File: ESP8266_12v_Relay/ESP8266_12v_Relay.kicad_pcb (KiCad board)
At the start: 2 copper layers, 71.9 x 40.9 mm, 41 parts, among them J1 691137710002, J2 691137710002, J3 691137710002, J4 691137710002, J5 Conn_01x06_Female, J6 691137710002, U1 ESP-WROOM-02D_M1102H3200PH3Q0_, U2 AP6502SP-13, U3 DMN2029USD-13, U4 DMN2029USD-13

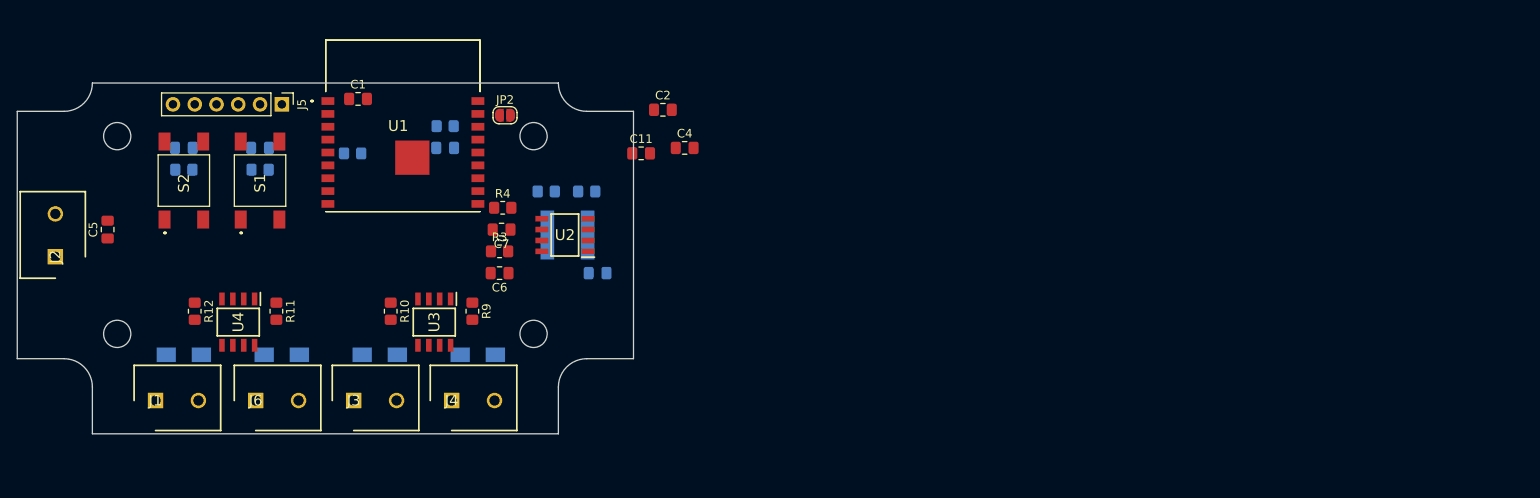
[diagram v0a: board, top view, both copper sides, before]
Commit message: Started 12v relay design
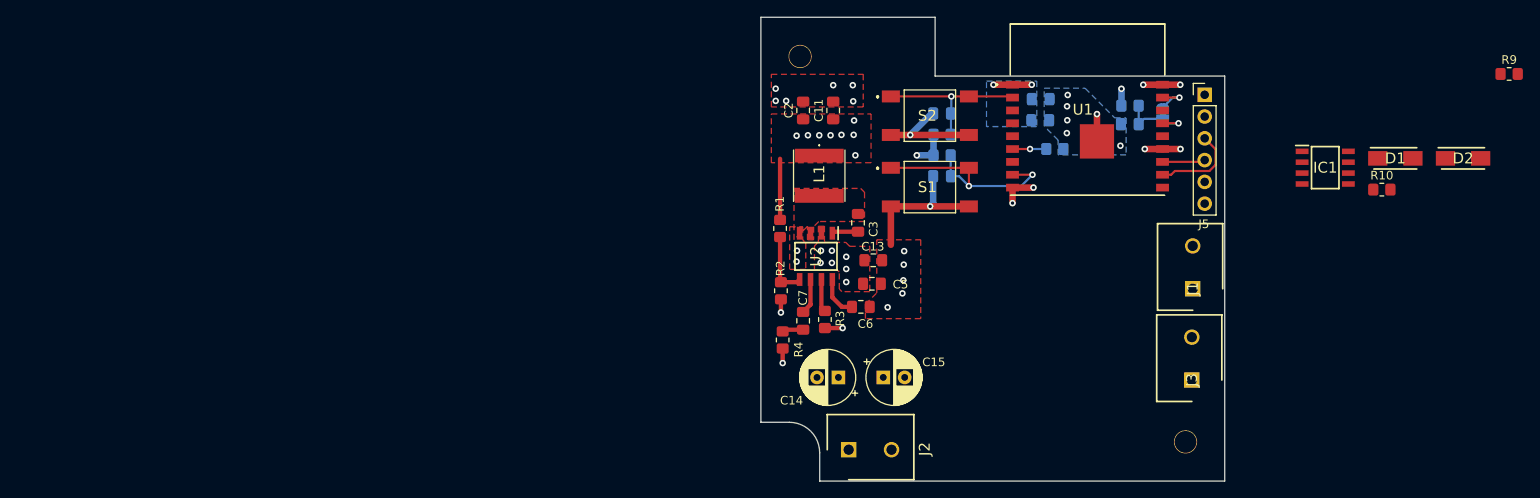
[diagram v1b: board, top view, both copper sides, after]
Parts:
- removed D3, D4: FM4004W-W, SamacSys_Parts:DIOM5025X231N
- removed J4, J6: 691137710002, SamacSys_Parts:SHDR2W70P0X500_1X2_1000X750X1160P
- removed R11, R12: 10k, Resistor_SMD:R_0805_2012Metric_Pad1.20x1.40mm_HandSolder
- removed U3, U4: DMN2029USD-13, SamacSys_Parts:SOIC127P600X175-8N
- added C13: 10uF, Capacitor_SMD:C_0805_2012Metric_Pad1.18x1.45mm_HandSolder, F.Cu at (216.3, 104.5)
- added C14: 100uF, Capacitor_THT:CP_Radial_D6.3mm_P2.50mm, F.Cu at (212.2, 118.2)
- added C15: 100uF, Capacitor_THT:CP_Radial_D6.3mm_P2.50mm, F.Cu at (217.5, 118.2)
- added H1: MountingHole, MountingHole:MountingHole_2.7mm_M2.5, F.Cu at (207.8, 80.8)
- added H2: MountingHole, MountingHole:MountingHole_2.7mm_M2.5, F.Cu at (252.7, 125.7)
- added IC1: DMN2029USD-13, SamacSys_Parts:SOIC127P600X175-8N, F.Cu at (269.0, 93.7)
- C1, C4, JP2: moved to B.Cu
- C11: value 10uF -> 22uF
- C3, D1, D2, L1, R1, R2: moved to F.Cu
- moved D1 143.2 mm to (277.2, 92.7)
- moved D2 139.7 mm to (285.1, 92.7)
- moved R9 124.1 mm to (290.5, 82.8), turned to 0 degrees
- moved J1 121.7 mm to (253.6, 107.9), turned to 90 degrees
- moved R10 116.5 mm to (275.6, 96.3), turned to 0 degrees
- moved J5 107.7 mm to (255.0, 85.2), turned to 0 degrees
- moved J3 97.8 mm to (253.5, 118.5), turned to 90 degrees
- moved J2 95.2 mm to (213.4, 126.6), turned to 0 degrees
- moved C5 89.4 mm to (216.2, 107.3), turned to 0 degrees
- moved R5 88.5 mm to (224.3, 89.9)
- moved C8 88.5 mm to (224.3, 87.4), turned to 180 degrees
- moved S2 87.3 mm to (222.9, 87.7), turned to 0 degrees
- moved R8 81.9 mm to (237.5, 91.6)
- moved R6 79.9 mm to (246.3, 86.5)
- moved C9 79.9 mm to (246.2, 88.7)
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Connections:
- net /ESP_TOUT renamed /TOUT
- C11 pad 1: +12V -> +3V3
- J1 pad 2: /PWM3_D -> /PWM0_D
- U1 pad 6: /PWM2 -> /GPIO15
- U1 pad 7: /PWM3 -> /GPIO2
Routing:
- net GND: track 0.00 -> 49.2 mm, vias 0 -> 29
- net /GPIO0: track 0.00 -> 26.5 mm, vias 0 -> 2
- net /ESP_EN: track 0.00 -> 18.7 mm, vias 0 -> 1
- net +3V3: track 0.00 -> 17.9 mm, vias 0 -> 12
- net /ESP_RXD: track 0.00 -> 10.3 mm
- net /ESP_RST_L: track 0.00 -> 9.15 mm, vias 0 -> 1
- net /U2_FB: track 0.00 -> 7.62 mm
- net /ESP_TXD: track 0.00 -> 5.00 mm
- net /U2_SS: track 0.00 -> 4.83 mm
- net /GPIO16: track 0.00 -> 4.41 mm, vias 0 -> 1
- net /U2_COMP: track 0.00 -> 4.14 mm
- net /GPIO15: track 0.00 -> 3.94 mm, vias 0 -> 1
- net /U2_EN: track 0.00 -> 3.83 mm
- net /U2_BST: track 0.00 -> 3.07 mm
- net Net-(C7-Pad2): track 0.00 -> 2.47 mm
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- added copper zone on F.Cu, net +12V
- added copper zone on In2.Cu, net +12V
- added copper zone on B.Cu, net +3V3
- added copper zone on F.Cu, net +3V3
- added copper zone on In2.Cu, net +3V3
- added copper zone on F.Cu, net /U2_SW
- added copper zone on B.Cu, net GND
- added copper zone on F.Cu, net GND
- added copper zone on In1.Cu, net GND
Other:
- board size 71.9 x 40.9 mm -> 54.1 x 54.1 mm
- copper layers 2 -> 4
- net class Default: clearance 0.1524 -> 0.254; trace_width 0.1524 -> 0.254; via_dia 0.508 -> 0.5588
- net class Power added: clearance 0.508, trace_width 0.508, via_dia 0.762, via_drill 0.508
- rule trace_clearance: 0.1524 -> 0.254
- rule trace_min: 0.1524 -> 0.254
- rule via_min_size: 0.508 -> 0.5588
- board text removed: "Adafruit MPU6050"

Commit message: Finished 12v relay layout
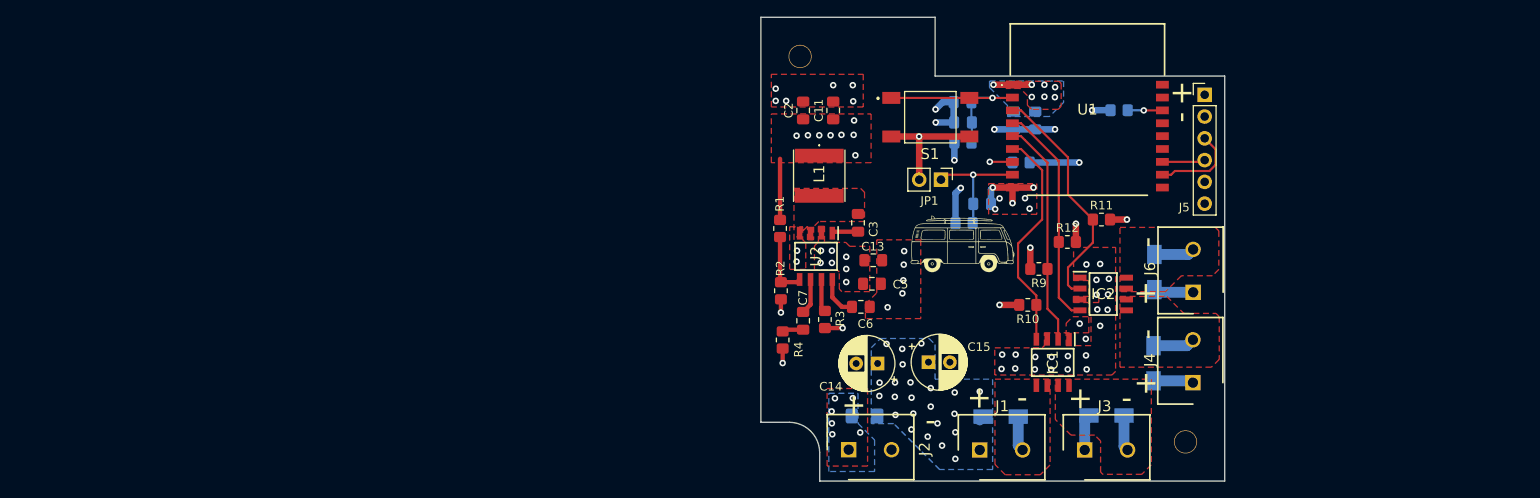
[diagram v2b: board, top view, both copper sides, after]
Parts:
- removed JP2: SolderJumper_2_Open, Jumper:SolderJumper-2_P1.3mm_Open_RoundedPad1.0x1.5mm
- removed S2: LL3301NF065QG, SamacSys_Parts:LL3301NF065QG
- added D3: FM4004W-W, SamacSys_Parts:DIOM5025X231N, B.Cu at (249.1, 105.9)
- added D4: FM4004W-W, SamacSys_Parts:DIOM5025X231N, B.Cu at (249.0, 116.6)
- added F1: 5A, Fuse:Fuse_1206_3216Metric_Pad1.42x1.75mm_HandSolder, B.Cu at (215.3, 122.7)
- added G1: Van_Graphic, SamacSys_Parts:van_pic, F.Cu at (226.7, 102.6)
- added IC2: DMN2029USD-13, SamacSys_Parts:SOIC127P600X175-8N, F.Cu at (243.1, 108.5)
- added J4: 691137710002, SamacSys_Parts:SHDR2W70P0X500_1X2_1000X750X1160P, F.Cu at (253.6, 118.8)
- added J6: 691137710002, SamacSys_Parts:SHDR2W70P0X500_1X2_1000X750X1160P, F.Cu at (253.6, 108.3)
- added JP1: Jumper_2_Open, Connector_PinHeader_2.54mm:PinHeader_1x02_P2.54mm_Vertical, F.Cu at (224.2, 95.1)
- added R11: 10k, Resistor_SMD:R_0805_2012Metric_Pad1.20x1.40mm_HandSolder, F.Cu at (242.9, 99.8)
- added R12: 10k, Resistor_SMD:R_0805_2012Metric_Pad1.20x1.40mm_HandSolder, F.Cu at (238.9, 102.4)
- C8: value 0.1uF -> 1uF
- D1, D2: moved to B.Cu
- U1: value ESP-WROOM-02D_M1102H3200PH3Q0_ -> ESP32-C3-WROOM-02-H4; footprint SamacSys_Parts:ESPWROOM02DM1102H3200PH3Q0 -> SamacSys_Parts:ESP32C3WROOM02H4
- moved D2 61.8 mm to (231.2, 122.8)
- moved R9 59.4 mm to (235.6, 105.6), turned to 180 degrees
- moved D1 45.1 mm to (243.5, 122.7)
- moved R10 43.4 mm to (234.3, 109.8), turned to 180 degrees
- moved IC1 39.1 mm to (237.2, 116.5), turned to 270 degrees
- moved J1 26.0 mm to (228.7, 126.7), turned to 0 degrees
- moved J3 22.6 mm to (241.0, 126.7), turned to 0 degrees
- moved R5 20.8 mm to (245.0, 87.0)
- moved C9 19.7 mm to (226.7, 86.1)
- moved R6 14.3 mm to (233.6, 93.1), turned to 180 degrees
- moved U1 13.8 mm to (231.8, 97.0)
- moved R8 10.7 mm to (226.8, 90.8)
- moved R7 8.31 mm to (226.9, 100.2)
- moved S1 8.15 mm to (223.0, 87.9)
- moved C10 5.68 mm to (229.0, 98.0), turned to 0 degrees
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- renumbered J3 to J1, J1 to J3
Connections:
- net /GPIO4 renamed /GPIO10_NC
- net /GPIO5 renamed /GPIO19_NC
- C10 pad 1: /GPIO0 -> /GPIO9
- C9 pad 1: /ESP_RST_L -> /ESP_EN
- D1 pad 2: /PWM0_D -> /PWM1_D
- D2 pad 2: /PWM1_D -> /PWM0_D
- IC1 pad 2: /PWM0 -> /PWM1
- IC1 pad 4: /PWM1 -> /PWM0
- IC1 pad 5: /PWM1_D -> /PWM0_D
- IC1 pad 6: /PWM1_D -> /PWM0_D
- IC1 pad 7: /PWM0_D -> /PWM1_D
- IC1 pad 8: /PWM0_D -> /PWM1_D
- J1 pad 2: /PWM1_D -> /PWM0_D
- J2 pad 1: +12V -> Net-(F1-Pad1)
- J3 pad 2: /PWM0_D -> /PWM1_D
- R10 pad 1: /PWM1 -> /PWM0
- R5 pad 2: /ESP_EN -> /GPIO2
- R6 pad 2: /ESP_RST_L -> /GPIO8
- R7 pad 2: /GPIO0 -> /GPIO9
- R8 pad 1: /GPIO15 -> +3V3
- R8 pad 2: GND -> /ESP_EN
- R9 pad 1: /PWM0 -> /PWM1
- S1 pad 1: /GPIO0 -> /ESP_EN
- S1 pad 2: /GPIO0 -> /ESP_EN
- U1 pad 13: GND -> /GPIO18_NC
- U1 pad 15: /ESP_RST_L -> /GPIO3_NC
- U1 pad 16: /TOUT -> /GPIO2
- U1 pad 17: /GPIO16 -> /GPIO1_NC
- U1 pad 18: GND -> /GPIO0_NC
- U1 pad 3: /GPIO14 -> /PWM3
- U1 pad 4: /PWM0 -> /PWM2
- U1 pad 6: /GPIO15 -> /PWM0
- U1 pad 7: /GPIO2 -> /GPIO8
- U1 pad 8: /GPIO0 -> /GPIO9
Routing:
- net /PWM3: track 0.00 -> 27.6 mm
- net /GPIO0: track 26.5 -> 0.00 mm, vias 2 -> 0
- net /PWM1: track 0.00 -> 26.5 mm
- net /PWM0: track 0.00 -> 26.3 mm
- net /PWM2: track 0.00 -> 26.3 mm
- net /GPIO9: track 0.00 -> 14.4 mm, vias 0 -> 1
- net +12V: track 2.07 -> 16.2 mm, vias 8 -> 31
- net /ESP_RST_L: track 9.15 -> 0.00 mm, vias 1 -> 0
- net +3V3: track 17.9 -> 25.9 mm, vias 12 -> 19
- net /PWM2_D: track 0.00 -> 4.88 mm
- net /PWM3_D: track 0.00 -> 4.76 mm
- net /GPIO16: track 4.41 -> 0.00 mm, vias 1 -> 0
- net /PWM1_D: track 0.00 -> 4.18 mm
- net /PWM0_D: track 0.00 -> 4.10 mm
- net /GPIO2: track 0.00 -> 4.06 mm, vias 0 -> 1
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- added copper zone on B.Cu, net +12V
- added copper zone on F.Cu, net /PWM0_D
- added copper zone on F.Cu, net /PWM1_D
- added copper zone on F.Cu, net /PWM2_D
- added copper zone on F.Cu, net /PWM3_D
- added copper zone on B.Cu, net Net-(F1-Pad1)
- added copper zone on F.Cu, net Net-(F1-Pad1)
- removed copper zone on B.Cu, net GND
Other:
- board text added: "+"
- board text added: "-"

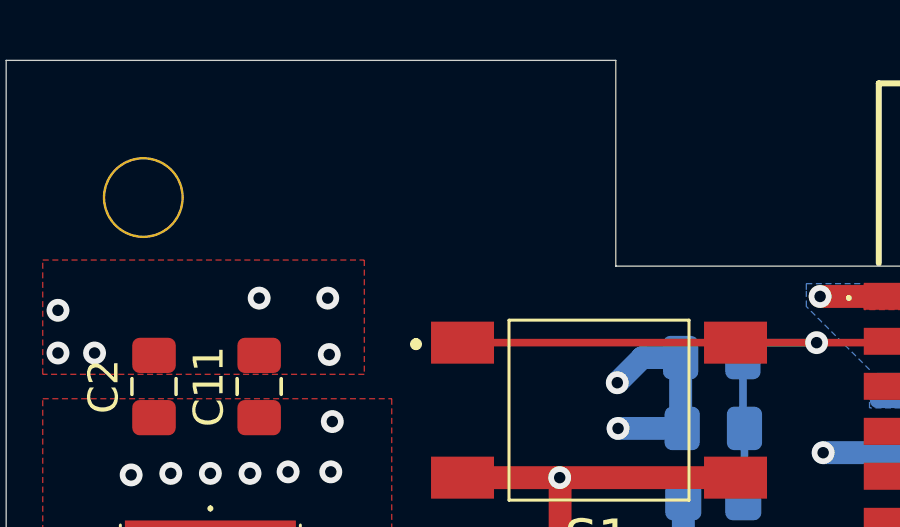
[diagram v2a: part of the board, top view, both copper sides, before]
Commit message: Added LEDs to 12v relay
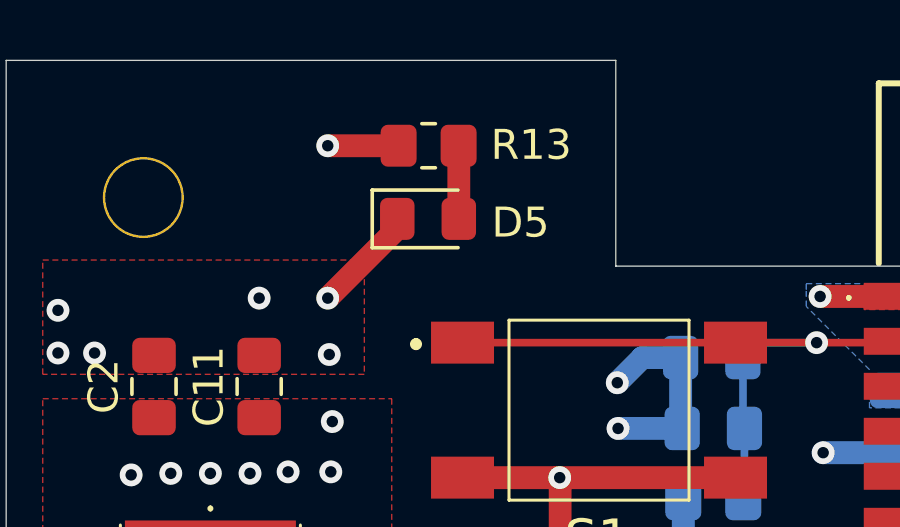
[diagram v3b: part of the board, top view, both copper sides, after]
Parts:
- added D5: LED, LED_SMD:LED_0805_2012Metric_Pad1.15x1.40mm_HandSolder, F.Cu at (217.3, 81.5)
- added R13: 66.5, Resistor_SMD:R_0805_2012Metric_Pad1.20x1.40mm_HandSolder, F.Cu at (217.3, 79.0)
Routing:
- net GND: track 48.9 -> 52.5 mm
- net Net-(D5-Pad2): track 0.00 -> 2.44 mm
- net +3V3: track 25.9 -> 28.3 mm, vias 19 -> 20
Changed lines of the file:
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@@
     (thickness 1.6002)
     (drawings 21)
-    (tracks 267)
+    (tracks 274)
     (zones 0)
-    (modules 47)
-    (nets 34)
+    (modules 49)
+    (nets 35)
   )
   (page A4)
@@
   (net 32 /GPIO0_NC)
   (net 33 "Net-(F1-Pad1)")
+  (net 34 "Net-(D5-Pad2)")
   (net_class Default "This is the default net class."
     (clearance 0.254)
@@
     (add_net /U2_SW)
     (add_net "Net-(C7-Pad2)")
+    (add_net "Net-(D5-Pad2)")
   )
   (net_class Power ""
@@
       (xy -3.500766 -3.282122)) (layer F.SilkS) (width 0.01))
   )
+  (module LED_SMD:LED_0805_2012Metric_Pad1.15x1.40mm_HandSolder (layer F.Cu)
+    (at 217.2626 81.4832)
+    (descr "LED SMD 0805 (2012 Metric), square (rectangular) end terminal, IPC_7351 nominal, (Body size source: https://docs.google.com/spreadsheets/d/1BsfQQcO9C6DZCsRaXUlFlo91Tg2WpOkGARC1WS5S8t0/edit?usp=sharing), generated with kicad-footprint-generator")
+    (tags "LED handsolder")
+    (attr smd)
+    (fp_text reference D5 (at 3.0824 0.127) (layer F.SilkS)
+      (effects (font (size 1 1) (thickness 0.15)))
+    )
+    (fp_text value LED (at 0 1.65) (layer F.Fab)
+      (effects (font (size 1 1) (thickness 0.15)))
+    )
+    (fp_line (start 1.85 0.95) (end -1.85 0.95) (layer F.CrtYd) (width 0.05))
+    (fp_line (start 1.85 -0.95) (end 1.85 0.95) (layer F.CrtYd) (width 0.05))
+    (fp_line (start -1.85 -0.95) (end 1.85 -0.95) (layer F.CrtYd) (width 0.05))
+    (fp_line (start -1.85 0.95) (end -1.85 -0.95) (layer F.CrtYd) (width 0.05))
+    (fp_line (start -1.86 0.96) (end 1 0.96) (layer F.SilkS) (width 0.12))
+    (fp_line (start -1.86 -0.96) (end -1.86 0.96) (layer F.SilkS) (width 0.12))
+    (fp_line (start 1 -0.96) (end -1.86 -0.96) (layer F.SilkS) (width 0.12))
+    (fp_line (start 1 0.6) (end 1 -0.6) (layer F.Fab) (width 0.1))
+    (fp_line (start -1 0.6) (end 1 0.6) (layer F.Fab) (width 0.1))
+    (fp_line (start -1 -0.3) (end -1 0.6) (layer F.Fab) (width 0.1))
+    (fp_line (start -0.7 -0.6) (end -1 -0.3) (layer F.Fab) (width 0.1))
+    (fp_line (start 1 -0.6) (end -0.7 -0.6) (layer F.Fab) (width 0.1))
+    (fp_text user %R (at 0 0) (layer F.Fab)
+      (effects (font (size 0.5 0.5) (thickness 0.08)))
+    )
+    (pad 1 smd roundrect (at -1.025 0) (size 1.15 1.4) (layers F.Cu F.Paste F.Mask) (roundrect_rratio 0.217391)
+      (net 2 GND))
+    (pad 2 smd roundrect (at 1.025 0) (size 1.15 1.4) (layers F.Cu F.Paste F.Mask) (roundrect_rratio 0.217391)
+      (net 34 "Net-(D5-Pad2)"))
+    (model ${KISYS3DMOD}/LED_SMD.3dshapes/LED_0805_2012Metric.wrl
+      (at (xyz 0 0 0))
+      (scale (xyz 1 1 1))
+      (rotate (xyz 0 0 0))
+    )
+  )
+  (module Resistor_SMD:R_0805_2012Metric_Pad1.20x1.40mm_HandSolder (layer F.Cu)
+    (at 217.281 79.0448)
+    (descr "Resistor SMD 0805 (2012 Metric), square (rectangular) end terminal, IPC_7351 nominal with elongated pad for handsoldering. (Body size source: IPC-SM-782 page 72, https://www.pcb-3d.com/wordpress/wp-content/uploads/ipc-sm-782a_amendment_1_and_2.pdf), generated with kicad-footprint-generator")
+    (tags "resistor handsolder")
+    (attr smd)
+    (fp_text reference R13 (at 3.4196 -0.0254) (layer F.SilkS)
+      (effects (font (size 1 1) (thickness 0.15)))
+    )
+    (fp_text value 66.5 (at 0 1.65) (layer F.Fab)
+      (effects (font (size 1 1) (thickness 0.15)))
+    )
+    (fp_line (start 1.85 0.95) (end -1.85 0.95) (layer F.CrtYd) (width 0.05))
+    (fp_line (start 1.85 -0.95) (end 1.85 0.95) (layer F.CrtYd) (width 0.05))
+    (fp_line (start -1.85 -0.95) (end 1.85 -0.95) (layer F.CrtYd) (width 0.05))
+    (fp_line (start -1.85 0.95) (end -1.85 -0.95) (layer F.CrtYd) (width 0.05))
+    (fp_line (start -0.227064 0.735) (end 0.227064 0.735) (layer F.SilkS) (width 0.12))
+    (fp_line (start -0.227064 -0.735) (end 0.227064 -0.735) (layer F.SilkS) (width 0.12))
+    (fp_line (start 1 0.625) (end -1 0.625) (layer F.Fab) (width 0.1))
+    (fp_line (start 1 -0.625) (end 1 0.625) (layer F.Fab) (width 0.1))
+    (fp_line (start -1 -0.625) (end 1 -0.625) (layer F.Fab) (width 0.1))
+    (fp_line (start -1 0.625) (end -1 -0.625) (layer F.Fab) (width 0.1))
+    (fp_text user %R (at 0 0) (layer F.Fab)
+      (effects (font (size 0.5 0.5) (thickness 0.08)))
+    )
+    (pad 1 smd roundrect (at -1 0) (size 1.2 1.4) (layers F.Cu F.Paste F.Mask) (roundrect_rratio 0.208333)
+      (net 1 +3V3))
+    (pad 2 smd roundrect (at 1 0) (size 1.2 1.4) (layers F.Cu F.Paste F.Mask) (roundrect_rratio 0.208333)
+      (net 34 "Net-(D5-Pad2)"))
+    (model ${KISYS3DMOD}/Resistor_SMD.3dshapes/R_0805_2012Metric.wrl
+      (at (xyz 0 0 0))
+      (scale (xyz 1 1 1))
+      (rotate (xyz 0 0 0))
+    )
+  )
   (gr_text - (at 252.1204 87.8586 90) (layer F.SilkS)
     (effects (font (size 2.54 2.54) (thickness 0.15)))
@@
   (segment (start 226.5172 96.1136) (end 226.5172 96.1136) (width 0.762) (layer B.Cu) (net 1))
   (via (at 226.5172 96.1136) (size 0.762) (drill 0.381) (layers F.Cu B.Cu) (net 1))
+  (segment (start 216.281 79.0448) (end 213.9188 79.0448) (width 0.762) (layer F.Cu) (net 1))
+  (segment (start 213.9188 79.0448) (end 213.9188 79.0448) (width 0.762) (layer F.Cu) (net 1))
+  (via (at 213.9188 79.0448) (size 0.762) (drill 0.381) (layers F.Cu B.Cu) (net 1))
   (segment (start 205.5368 109.1024) (end 205.5368 110.6424) (width 0.508) (layer F.Cu) (net 2))
   (segment (start 205.5368 110.6424) (end 205.5368 110.6424) (width 0.508) (layer F.Cu) (net 2))
@@
   (via (at 231.0384 97.3328) (size 0.762) (drill 0.381) (layers F.Cu B.Cu) (net 2))
   (via (at 234.5436 98.5266) (size 0.762) (drill 0.381) (layers F.Cu B.Cu) (net 2))
+  (segment (start 216.2376 81.806) (end 213.9188 84.1248) (width 0.762) (layer F.Cu) (net 2))
+  (segment (start 216.2376 81.4832) (end 216.2376 81.806) (width 0.762) (layer F.Cu) (net 2))
   (segment (start 210.6676 112.4552) (end 212.7344 112.4552) (width 0.508) (layer F.Cu) (net 3))
   (segment (start 212.7344 112.4552) (end 212.7344 112.4552) (width 0.508) (layer F.Cu) (net 3))
@@
   (via (at 214.7824 124.6378) (size 0.762) (drill 0.381) (layers F.Cu B.Cu) (net 33))
   (via (at 211.5312 124.841) (size 0.762) (drill 0.381) (layers F.Cu B.Cu) (net 33))
+  (segment (start 218.2876 79.0514) (end 218.281 79.0448) (width 0.762) (layer F.Cu) (net 34))
+  (segment (start 218.2876 81.4832) (end 218.2876 79.0514) (width 0.762) (layer F.Cu) (net 34))
   (zone (net 2) (net_name GND) (layer In1.Cu) (hatch edge 0.508)
     (connect_pads (clearance 0.508))
